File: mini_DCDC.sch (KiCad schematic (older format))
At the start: 19 parts, among them J1 Pin, J2 Pin, J3 Pin, J4 Pin, J5 Pin, U1 MC34063AD

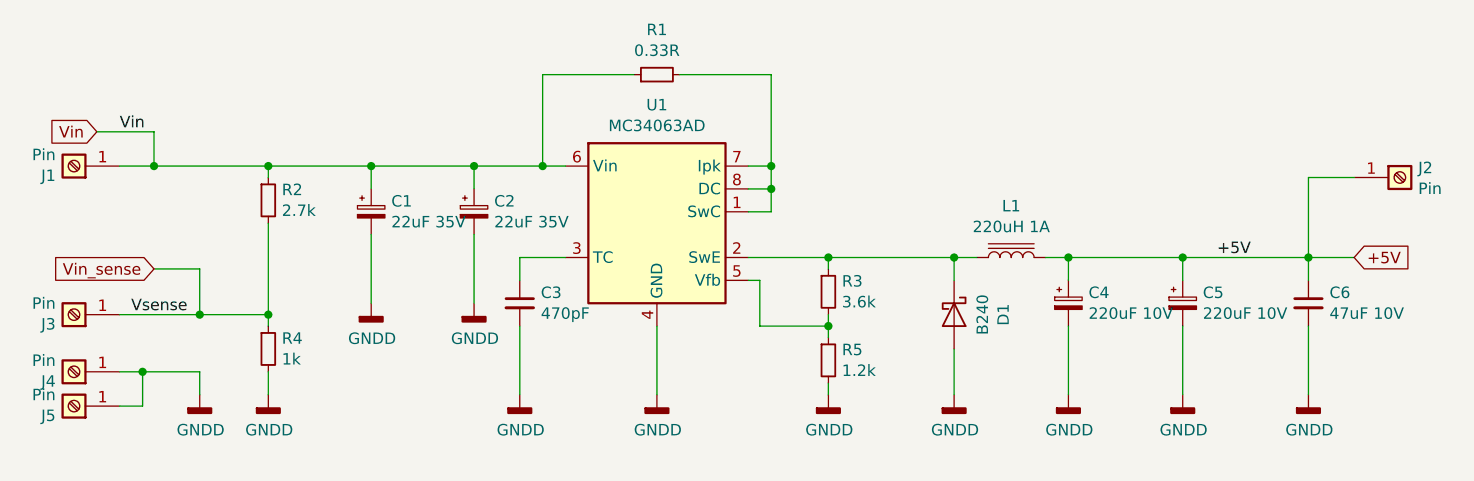
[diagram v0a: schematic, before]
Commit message: - Исправлена ошибка с неправильным подключением цепи обратной связи; - Увеличена длина платы на 2 мм; - Плата переразведена с учетом изменений в схеме;
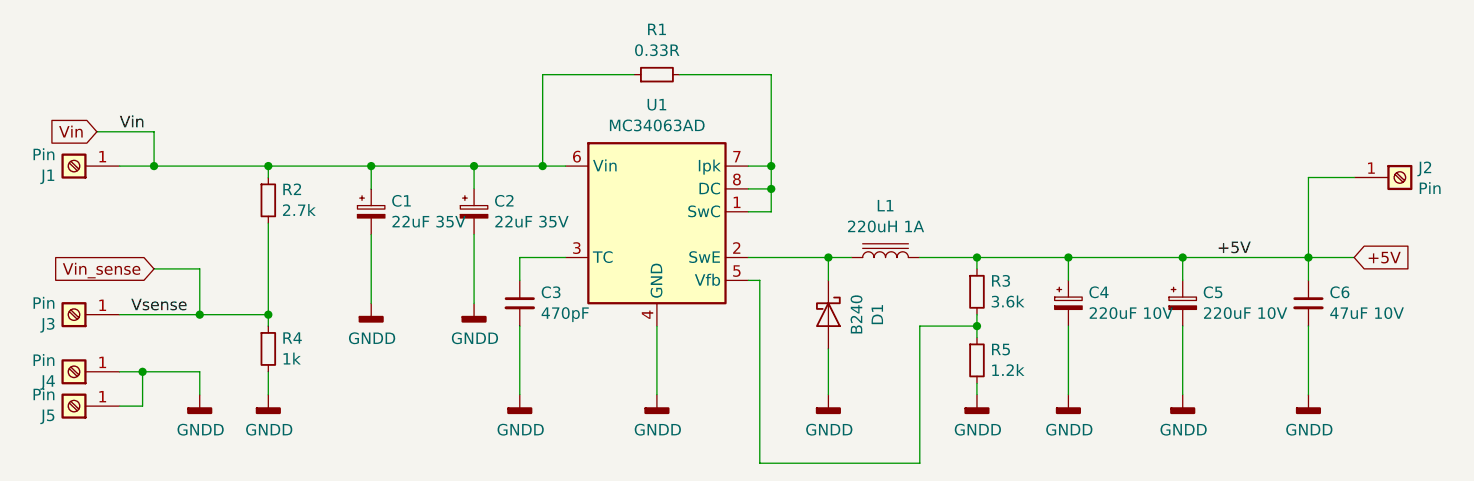
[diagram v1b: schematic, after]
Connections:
- net +5V: now also R3.1
- net at D1.1 (K), L1.1, U1.2 (SwE): no longer R3.1
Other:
- moved on the sheet: D1, L1, R3, R5
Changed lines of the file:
@@
 EESchema Schematic File Version 4
+LIBS:mini_DCDC-cache
 EELAYER 26 0
 EELAYER END
@@
 $EndComp
 Wire Wire Line
-	5400 2600 5750 2600
-Wire Wire Line
-	6300 2600 6300 2700
+	5750 2600 5750 2700
 Wire Wire Line
 	5400 2200 5500 2200
@@
 L Device:L_Core_Iron L1
 U 1 1 5BC4AB9C
-P 6550 2600
-F 0 "L1" V 6775 2600 50  0000 C CNN
-F 1 "220uH 1A" V 6684 2600 50  0000 C CNN
-F 2 "extras:SRR1208" H 6550 2600 50  0001 C CNN
-F 3 "~" H 6550 2600 50  0001 C CNN
-F 4 "SRR1208-221KL" V 6550 2600 50  0001 C CNN "partnum"
-	1    6550 2600
+P 6000 2600
+F 0 "L1" V 6225 2600 50  0000 C CNN
+F 1 "220uH 1A" V 6134 2600 50  0000 C CNN
+F 2 "extras:SRR1208" H 6000 2600 50  0001 C CNN
+F 3 "~" H 6000 2600 50  0001 C CNN
+F 4 "SRR1208-221KL" V 6000 2600 50  0001 C CNN "partnum"
+	1    6000 2600
 	0    -1   -1   0
 $EndComp
 Wire Wire Line
-	6300 2600 6400 2600
-Connection ~ 6300 2600
+	5750 2600 5850 2600
 $Comp
 L Device:CP_Small C4
@@
 	1    0    0    -1
 $EndComp
-Wire Wire Line
-	6700 2600 6800 2600
 $Comp
 L power:GNDD #PWR08
 U 1 1 5BC4B117
-P 6300 3200
-F 0 "#PWR08" H 6300 2950 50  0001 C CNN
-F 1 "GNDD" H 6304 3045 50  0000 C CNN
-F 2 "" H 6300 3200 50  0001 C CNN
-F 3 "" H 6300 3200 50  0001 C CNN
-	1    6300 3200
+P 5750 3200
+F 0 "#PWR08" H 5750 2950 50  0001 C CNN
+F 1 "GNDD" H 5754 3045 50  0000 C CNN
+F 2 "" H 5750 3200 50  0001 C CNN
+F 3 "" H 5750 3200 50  0001 C CNN
+	1    5750 3200
 	1    0    0    -1
 $EndComp
@@
 L Device:R_Small R3
 U 1 1 5BC4C84A
-P 5750 2750
-F 0 "R3" H 5809 2796 50  0000 L CNN
-F 1 "3.6k" H 5809 2705 50  0000 L CNN
-F 2 "Resistor_SMD:R_0805_2012Metric_Pad1.15x1.40mm_HandSolder" H 5750 2750 50  0001 C CNN
-F 3 "~" H 5750 2750 50  0001 C CNN
-F 4 "RC0805FR-072KL" H 5750 2750 50  0001 C CNN "partnum"
-	1    5750 2750
+P 6400 2750
+F 0 "R3" H 6459 2796 50  0000 L CNN
+F 1 "3.6k" H 6459 2705 50  0000 L CNN
+F 2 "Resistor_SMD:R_0805_2012Metric_Pad1.15x1.40mm_HandSolder" H 6400 2750 50  0001 C CNN
+F 3 "~" H 6400 2750 50  0001 C CNN
+F 4 "RC0805FR-072KL" H 6400 2750 50  0001 C CNN "partnum"
+	1    6400 2750
 	1    0    0    -1
 $EndComp
@@
 L Device:R_Small R5
 U 1 1 5BC4CB89
-P 5750 3050
-F 0 "R5" H 5809 3096 50  0000 L CNN
-F 1 "1.2k" H 5809 3005 50  0000 L CNN
-F 2 "Resistor_SMD:R_0805_2012Metric_Pad1.15x1.40mm_HandSolder" H 5750 3050 50  0001 C CNN
-F 3 "~" H 5750 3050 50  0001 C CNN
-F 4 "RC0805FR-071K2L" H 5750 3050 50  0001 C CNN "partnum"
-	1    5750 3050
-	1    0    0    -1
-$EndComp
-Wire Wire Line
-	6300 3000 6300 3200
+P 6400 3050
+F 0 "R5" H 6459 3096 50  0000 L CNN
+F 1 "1.2k" H 6459 3005 50  0000 L CNN
+F 2 "Resistor_SMD:R_0805_2012Metric_Pad1.15x1.40mm_HandSolder" H 6400 3050 50  0001 C CNN
+F 3 "~" H 6400 3050 50  0001 C CNN
+F 4 "RC0805FR-071K2L" H 6400 3050 50  0001 C CNN "partnum"
+	1    6400 3050
+	1    0    0    -1
+$EndComp
+Wire Wire Line
+	5750 3000 5750 3200
 Wire Wire Line
 	6800 2900 6800 3200
@@
 L power:GNDD #PWR07
 U 1 1 5BC4D3B2
-P 5750 3200
-F 0 "#PWR07" H 5750 2950 50  0001 C CNN
-F 1 "GNDD" H 5754 3045 50  0000 C CNN
-F 2 "" H 5750 3200 50  0001 C CNN
-F 3 "" H 5750 3200 50  0001 C CNN
-	1    5750 3200
-	1    0    0    -1
-$EndComp
-Wire Wire Line
-	5750 3150 5750 3200
-Wire Wire Line
-	5750 2850 5750 2900
-Wire Wire Line
-	5750 2650 5750 2600
-Connection ~ 5750 2600
-Wire Wire Line
-	5750 2600 6300 2600
-Wire Wire Line
-	5450 2900 5450 2700
-Connection ~ 5750 2900
-Wire Wire Line
-	5750 2900 5750 2950
+P 6400 3200
+F 0 "#PWR07" H 6400 2950 50  0001 C CNN
+F 1 "GNDD" H 6404 3045 50  0000 C CNN
+F 2 "" H 6400 3200 50  0001 C CNN
+F 3 "" H 6400 3200 50  0001 C CNN
+	1    6400 3200
+	1    0    0    -1
+$EndComp
+Wire Wire Line
+	6400 3150 6400 3200
+Wire Wire Line
+	6400 2650 6400 2600
 Wire Wire Line
 	5450 2700 5400 2700
-Wire Wire Line
-	5450 2900 5750 2900
 $Comp
 L Device:R_Small R1
@@
 L Diode:B240 D1
 U 1 1 5C49EDA2
-P 6300 2850
+P 5750 2850
 AR Path="/5C49EDA2" Ref="D1"  Part="1"
 AR Path="/5C0A300C/5C49EDA2" Ref="D?"  Part="1"
 AR Path="/5BC4A73F/5C49EDA2" Ref="D?"  Part="1"
-F 0 "D1" H 6300 3066 50  0000 C CNN
-F 1 "B240" H 6300 2975 50  0000 C CNN
-F 2 "Diode_SMD:D_SMB" H 6300 2675 50  0001 C CNN
-F 3 "http://www.jameco.com/Jameco/Products/ProdDS/1538777.pdf" H 6300 2850 50  0001 C CNN
-	1    6300 2850
+F 0 "D1" H 5750 3066 50  0000 C CNN
+F 1 "B240" H 5750 2975 50  0000 C CNN
+F 2 "Diode_SMD:D_SMB" H 5750 2675 50  0001 C CNN
+F 3 "http://www.jameco.com/Jameco/Products/ProdDS/1538777.pdf" H 5750 2850 50  0001 C CNN
+	1    5750 2850
 	0    1    1    0
 $EndComp
@@
 Wire Wire Line
 	2750 3100 3000 3100
+Wire Wire Line
+	6400 2850 6400 2900
+Wire Wire Line
+	6150 2600 6400 2600
+Connection ~ 6400 2600
+Wire Wire Line
+	6400 2600 6800 2600
+Wire Wire Line
+	5750 2600 5400 2600
+Connection ~ 5750 2600
+Wire Wire Line
+	5450 3500 6150 3500
+Wire Wire Line
+	6150 2900 6400 2900
+Connection ~ 6400 2900
+Wire Wire Line
+	6400 2900 6400 2950
+Wire Wire Line
+	5450 2700 5450 3500
+Wire Wire Line
+	6150 2900 6150 3500
 $EndSCHEMATC
